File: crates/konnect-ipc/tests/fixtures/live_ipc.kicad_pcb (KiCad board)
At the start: 2 copper layers, 160 x 100 mm, 4 parts

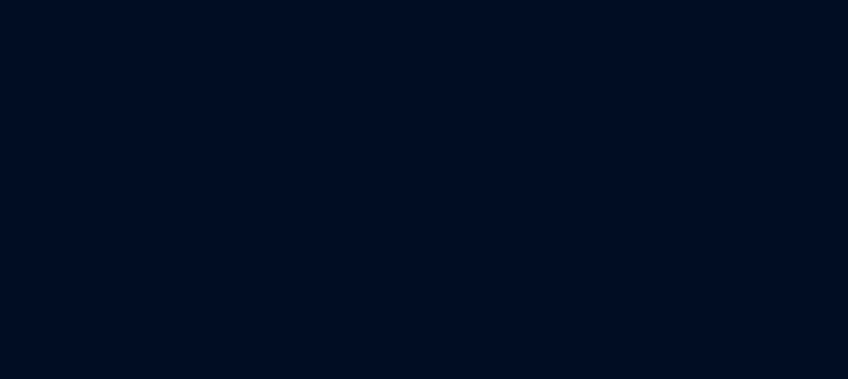
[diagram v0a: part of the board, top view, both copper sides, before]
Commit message: J.3.3: commit the live fixture's named net — the via test needs one
Run 32026034183 is clean of modals: the PCB Editor window is up, the API answers
in 0.34s instead of polling for 60, and `moving_and_rotating_footprint_preserves_
child_geometry` passes. The one failure is not about the runner at all —

    board has no named net to attach a via to

`live_ipc.kicad_pcb` gained a `(net 1 "GND")` and a segment on it, and those two
hunks were never committed, so the suite only ever passed against a working copy.
A runner clones what is pushed. Committed as-is.

Note for the record: this hunk predates this session's work — it was already in
the working tree — and is published here because the live test it feeds cannot
pass without it.

Co-Authored-By: Claude Opus 5 <noreply@anthropic.com>
Claude-Session: https://claude.ai/code/session_01HwsxFJXYLp8waGEHEpC9ej
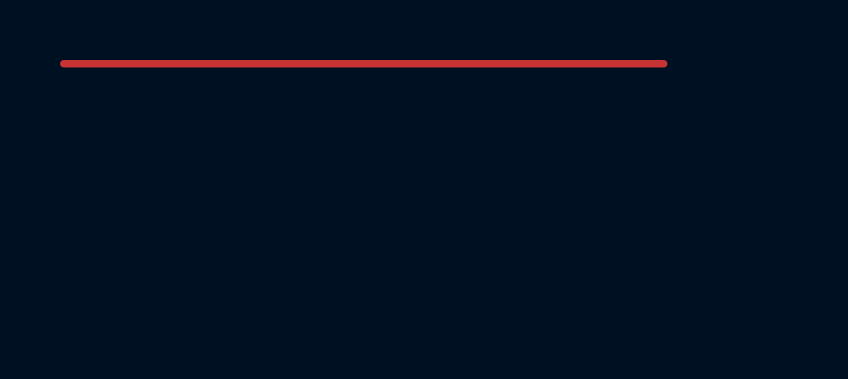
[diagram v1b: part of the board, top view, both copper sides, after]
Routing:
- net GND: track 0.00 -> 20.0 mm
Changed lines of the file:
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@@
 	)
 	(net 0 "")
+	(net 1 "GND")
 	(footprint "MountingHole:MountingHole_2.7mm_M2.5_DIN965"
 		(locked yes)
@@
 		)
 	)
+	(segment
+		(start 30 30)
+		(end 50 30)
+		(width 0.25)
+		(layer "F.Cu")
+		(net 1)
+	)
 	(embedded_fonts no)
